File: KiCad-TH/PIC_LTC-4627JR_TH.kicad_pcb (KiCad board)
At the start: 2 copper layers, 17 parts, among them J1 Conn_01x05_Male, J2 Conn_01x04, Q1 Q_NPN_EBC, Q2 Q_NPN_EBC, Q3 Q_NPN_EBC, Q4 Q_NPN_EBC, Q5 Q_NPN_EBC, U1 PIC16F18344-P

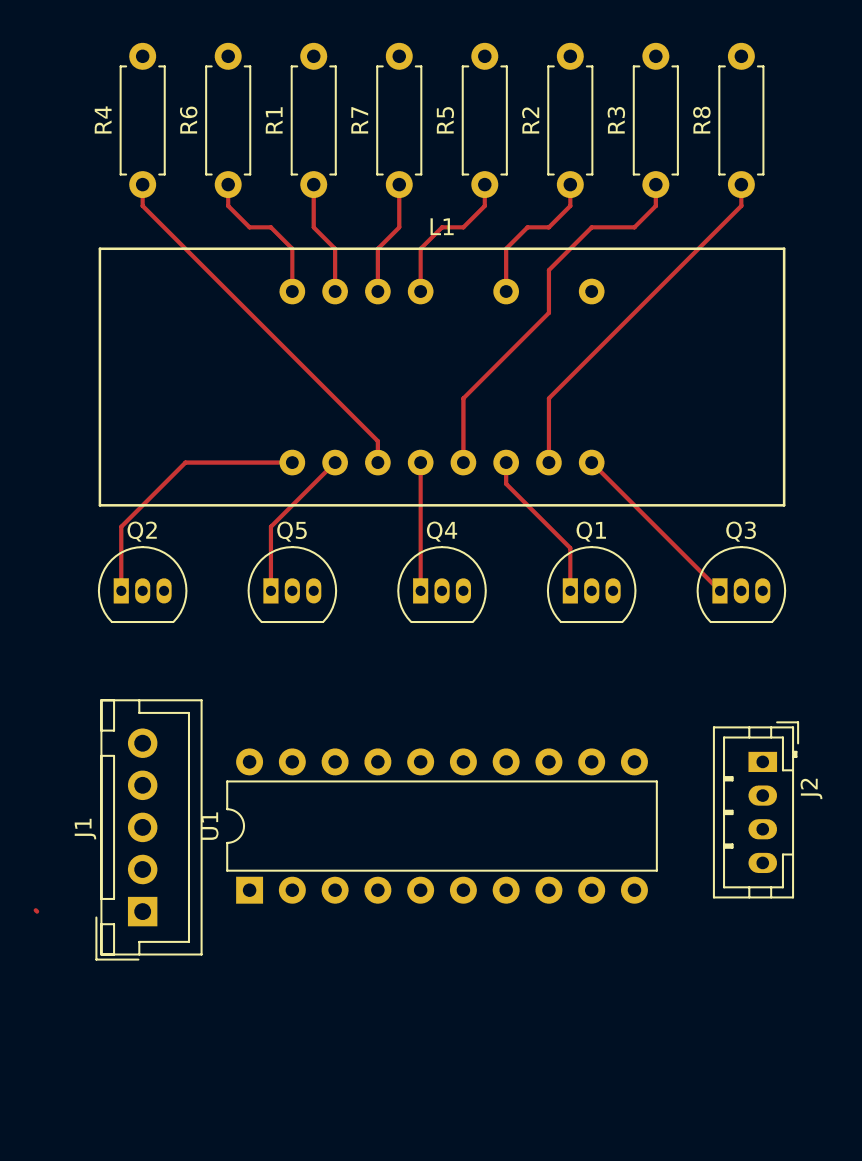
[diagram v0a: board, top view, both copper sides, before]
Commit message: Deleted all the tracks to start again.
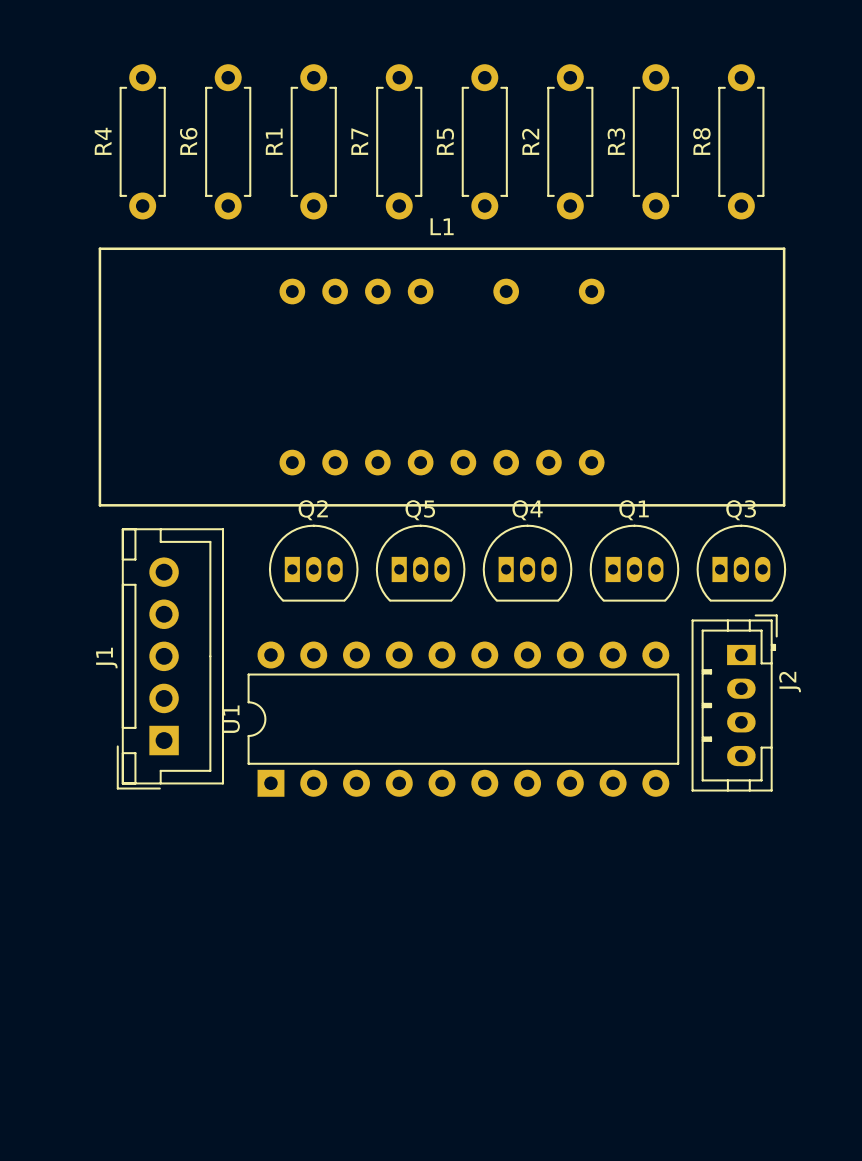
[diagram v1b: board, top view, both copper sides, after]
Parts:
- moved Q2 10.2 mm to (120.7, 104.1)
- moved J1 10.2 mm to (113.0, 114.3)
- moved Q5 7.73 mm to (127.0, 104.1)
- moved J2 6.48 mm to (147.3, 109.2)
- moved U1 6.48 mm to (119.4, 116.8)
- moved Q4 5.24 mm to (133.3, 104.1)
- moved Q1 2.84 mm to (139.7, 104.1)
- moved Q3 1.27 mm to (146.1, 104.1)
- moved R1 1.27 mm to (121.9, 82.5)
- moved R2 1.27 mm to (137.2, 82.5)
- moved R3 1.27 mm to (142.2, 82.5)
- moved R4 1.27 mm to (111.8, 82.5)
- moved R5 1.27 mm to (132.1, 82.5)
- moved R6 1.27 mm to (116.8, 82.5)
- moved R7 1.27 mm to (127.0, 82.5)
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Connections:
- J2 pad 1: VCC -> /I2CCL
- J2 pad 2: GND -> /I2CDA
- J2 pad 3: /I2CDA -> GND
- J2 pad 4: /I2CDL -> VCC
- U1 pad 11: /I2CDL -> /I2CCL
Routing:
- net Net-(L1-Pad5): track 22.7 -> 0.00 mm
- net Net-(L1-Pad3): track 22.3 -> 0.00 mm
- net Net-(L1-Pad7): track 21.2 -> 0.00 mm
- net /DIG_1: track 15.5 -> 0.00 mm
- net /DIG_4: track 10.8 -> 0.00 mm
- net /DIG_2: track 9.20 -> 0.00 mm
- net /DIG_3: track 9.20 -> 0.00 mm
- net Net-(L1-Pad13): track 8.67 -> 0.00 mm
- net Net-(L1-Pad16): track 8.67 -> 0.00 mm
- net Net-(L1-Pad11): track 8.67 -> 0.00 mm
- net /DIG_L: track 7.62 -> 0.00 mm
- net Net-(L1-Pad15): track 6.88 -> 0.00 mm
- net Net-(L1-Pad14): track 6.88 -> 0.00 mm

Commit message: Round 2: Not pretty, but at least it's all connected.
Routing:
- net Net-(Q1-Pad2): track 0.00 -> 111.6 mm
- net VCC: track 0.00 -> 109.7 mm
- net Net-(R7-Pad2): track 0.00 -> 87.1 mm
- net Net-(R4-Pad2): track 0.00 -> 66.3 mm
- net Net-(R8-Pad2): track 0.00 -> 52.1 mm
- net Net-(R6-Pad2): track 0.00 -> 48.1 mm
- net GND: track 0.00 -> 44.9 mm
- net Net-(R5-Pad2): track 0.00 -> 43.7 mm
- net Net-(R1-Pad2): track 0.00 -> 39.0 mm
- net Net-(R3-Pad2): track 0.00 -> 37.4 mm
- net Net-(Q3-Pad2): track 0.00 -> 37.0 mm
- net Net-(R2-Pad2): track 0.00 -> 36.4 mm
- net Net-(L1-Pad3): track 0.00 -> 21.0 mm
- net Net-(Q5-Pad2): track 0.00 -> 20.0 mm
- net Net-(L1-Pad7): track 0.00 -> 20.0 mm
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
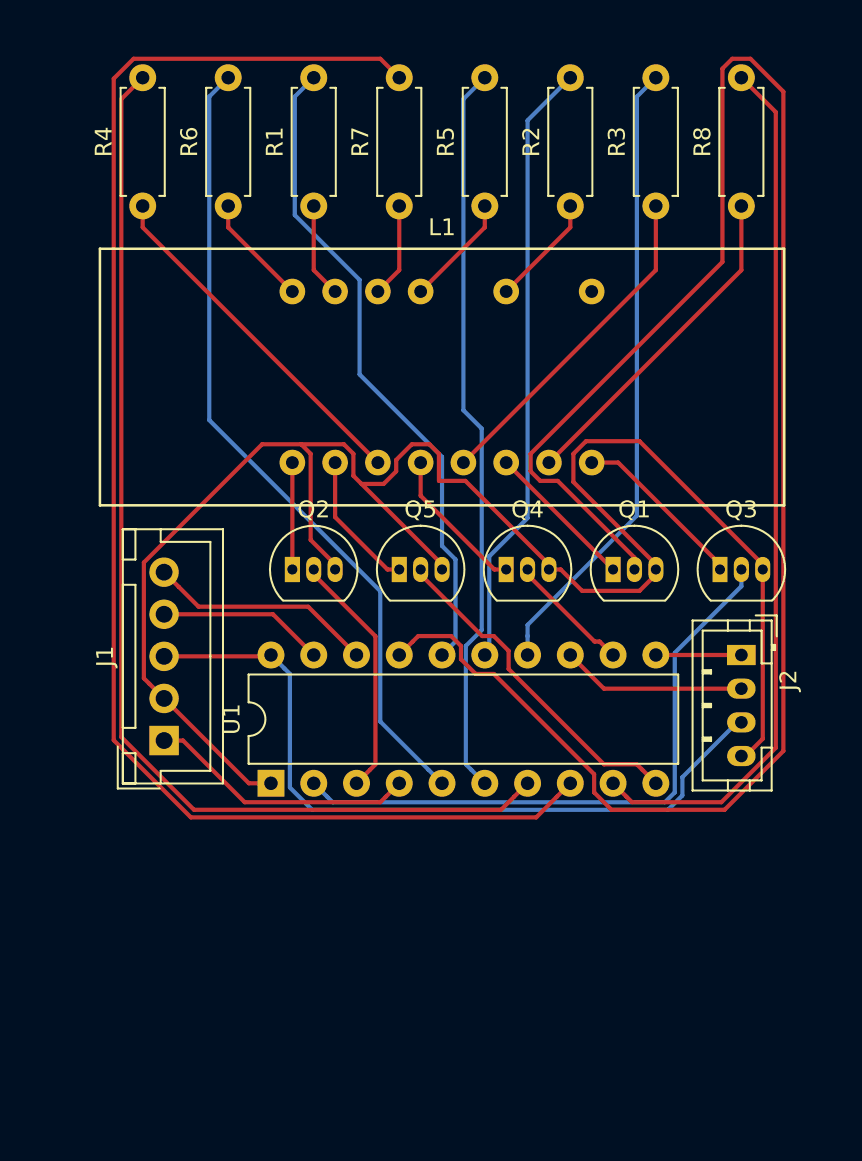
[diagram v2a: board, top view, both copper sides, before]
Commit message: Added edge, which highlighted lack of mounting holes.
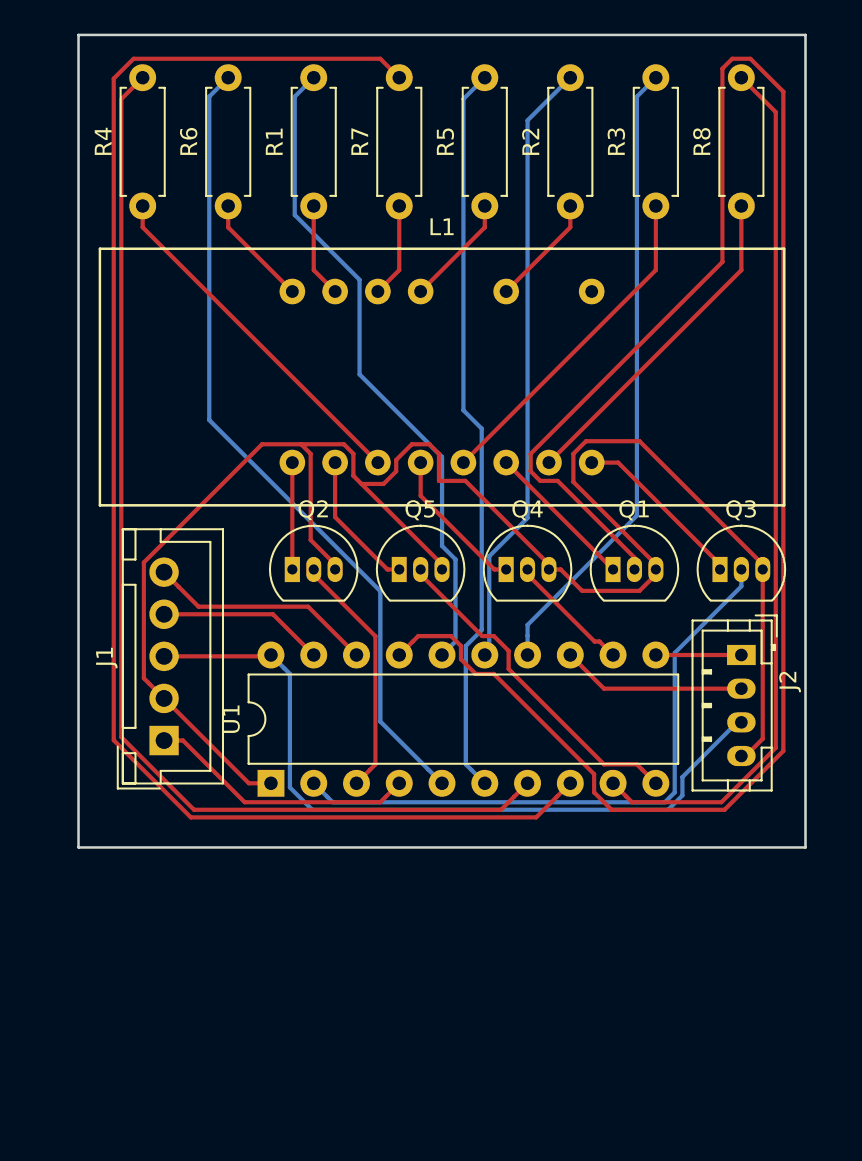
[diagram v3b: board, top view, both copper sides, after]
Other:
- board outline added: 43.2 x 48.3 mm
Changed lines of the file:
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@@
   (general
     (thickness 1.6)
-    (drawings 0)
+    (drawings 4)
     (tracks 195)
     (zones 0)
@@
     )
   )
+  (gr_line (start 107.95 120.65) (end 107.95 72.39) (layer Edge.Cuts) (width 0.15))
+  (gr_line (start 151.13 120.65) (end 107.95 120.65) (layer Edge.Cuts) (width 0.15))
+  (gr_line (start 151.13 72.39) (end 151.13 120.65) (layer Edge.Cuts) (width 0.15))
+  (gr_line (start 107.95 72.39) (end 151.13 72.39) (layer Edge.Cuts) (width 0.15))
   (segment (start 124.46 109.22) (end 121.58999 106.34999) (width 0.25) (layer F.Cu) (net 1))
   (segment (start 121.58999 106.34999) (end 115.07999 106.34999) (width 0.25) (layer F.Cu) (net 1))

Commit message: PCB Routing Round #3: Getting better, still room for improvement.
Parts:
- moved J2 40.3 mm to (111.8, 128.3), turned to 90 degrees
- moved J1 34.3 mm to (147.3, 115.6), turned to 270 degrees
- moved R4 28.7 mm to (132.1, 102.9), turned to 270 degrees
- moved U1 21.9 mm to (141.0, 120.7), turned to 270 degrees
- moved R1 20.9 mm to (116.8, 102.9), turned to 270 degrees
- moved R5 20.9 mm to (127.0, 102.9), turned to 270 degrees
- moved R6 20.9 mm to (111.8, 102.9), turned to 270 degrees
- moved R7 20.9 mm to (121.9, 102.9), turned to 270 degrees
- moved R3 20.9 mm to (147.3, 102.9), turned to 270 degrees
- moved R8 20.9 mm to (142.2, 102.9), turned to 270 degrees
- moved R2 20.3 mm to (137.2, 102.9), turned to 270 degrees
- moved Q3 13.5 mm to (137.2, 114.3), turned to 270 degrees
- moved Q2 13.5 mm to (111.8, 114.3), turned to 270 degrees
- moved Q4 13.5 mm to (124.5, 114.3), turned to 270 degrees
- moved Q5 13.5 mm to (118.1, 114.3), turned to 270 degrees
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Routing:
- net Net-(Q1-Pad2): track 111.6 -> 13.9 mm
- net Net-(R7-Pad2): track 87.1 -> 10.7 mm
- net Net-(R4-Pad2): track 66.3 -> 12.8 mm
- net Net-(R5-Pad2): track 43.7 -> 10.7 mm
- net Net-(Q3-Pad2): track 37.0 -> 5.78 mm
- net VCC: track 109.7 -> 134.1 mm
- net Net-(Q2-Pad2): track 14.7 -> 38.1 mm
- net Net-(R6-Pad2): track 48.1 -> 29.3 mm
- net Net-(R1-Pad2): track 39.0 -> 23.6 mm
- net Net-(L1-Pad5): track 20.0 -> 34.9 mm
- net Net-(Q5-Pad2): track 20.0 -> 6.15 mm
- net /DIG_L: track 8.86 -> 22.5 mm
- net Net-(L1-Pad3): track 21.0 -> 7.93 mm
- net Net-(L1-Pad7): track 20.0 -> 32.7 mm
- net /DIG_1: track 6.35 -> 18.9 mm
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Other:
- board outline removed

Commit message: PCB Routing Round #4: Submit Candidate 1
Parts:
- moved R8 30.5 mm to (111.8, 102.9)
- moved R6 25.4 mm to (137.2, 102.9)
- moved Q2 21.6 mm to (133.3, 114.3)
- moved R2 10.2 mm to (147.3, 102.9)
- moved R4 5.08 mm to (127.0, 102.9)
- moved R5 5.08 mm to (132.1, 102.9)
- moved R1 5.08 mm to (121.9, 102.9)
- moved R7 5.08 mm to (116.8, 102.9)
- moved R3 5.08 mm to (142.2, 102.9)
- moved Q1 3.81 mm to (127.0, 114.3)
- moved Q5 3.81 mm to (114.3, 114.3)
- moved Q4 3.81 mm to (120.7, 114.3)
- moved Q3 2.54 mm to (139.7, 114.3)
- moved J2 1.27 mm to (111.8, 127.0)
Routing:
- net Net-(R8-Pad2): track 56.9 -> 14.5 mm
- net Net-(Q2-Pad2): track 38.1 -> 6.31 mm
- net Net-(L1-Pad5): track 34.9 -> 17.5 mm
- net Net-(R6-Pad2): track 29.3 -> 13.5 mm
- net /DIG_1: track 18.9 -> 32.6 mm
- net VCC: track 134.1 -> 123.8 mm
- net Net-(L1-Pad7): track 32.7 -> 42.9 mm
- net GND: track 52.9 -> 43.1 mm
- net Net-(L1-Pad16): track 17.7 -> 26.4 mm
- net Net-(L1-Pad14): track 15.5 -> 23.2 mm
- net Net-(R3-Pad2): track 34.2 -> 26.8 mm
- net Net-(Q4-Pad2): track 18.7 -> 13.9 mm
- net Net-(L1-Pad11): track 15.5 -> 19.8 mm
- net /DIG_L: track 22.5 -> 18.6 mm
- net Net-(L1-Pad3): track 7.93 -> 4.34 mm
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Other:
- board outline added: 40.6 x 58.4 mm
- board text added: "1"
- board text added: "B"
- board text added: "C"
- board text added: "E"
- board text added: "GND"
- board text added: "I2CCL"
- board text added: "I2CDA"
- board text added: "ICSP"
- board text added: "ICSPCLK"
- board text added: "ICSPDAT"
- board text added: "LTC-4627JR"
- board text added: "LTC-4627JR Driver 2017/09/29"
- board text added: "PIC16F18345"
- board text added: "PWR I2C"
- board text added: "VCC"
- board text added: "VPP"
- board text added: "newscrewdriver.com"
